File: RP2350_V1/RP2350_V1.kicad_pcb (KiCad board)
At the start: 4 copper layers, 65.3 x 95.8 mm, 107 parts, among them IC1 DMP1045U-7, IC2 DMP1045U-7, IC3 DMP1045U-7, J1 Conn_01x04_Pin, J2 Conn_01x08_Socket, J3 USB_C_Receptacle_USB2.0_16P, J4 Conn_01x08_Socket, J5 Conn_01x08_Socket, J6 Conn_01x02_Pin, J7 Conn_01x04_Pin, SW1 PTS 647 SN50 SMTR2 LFS, SW10 PTS 647 SN50 SMTR2 LFS, SW11 PTS 647 SN50 SMTR2 LFS, SW12 PTS 647 SN50 SMTR2 LFS, SW13 PTS 647 SN50 SMTR2 LFS, SW14 PTS 647 SN50 SMTR2 LFS, SW4 PTS 647 SN50 SMTR2 LFS, SW9 PTS 647 SN50 SMTR2 LFS, U1 RP2350_60QFN, U2 W25Q128JVS, U3 TPS62811QWRWYRQ1, U4 MCP73812T-420I-OT, U5 TLV3012AIDCKR, U6 74HC14, X1 ABM8-272-T3

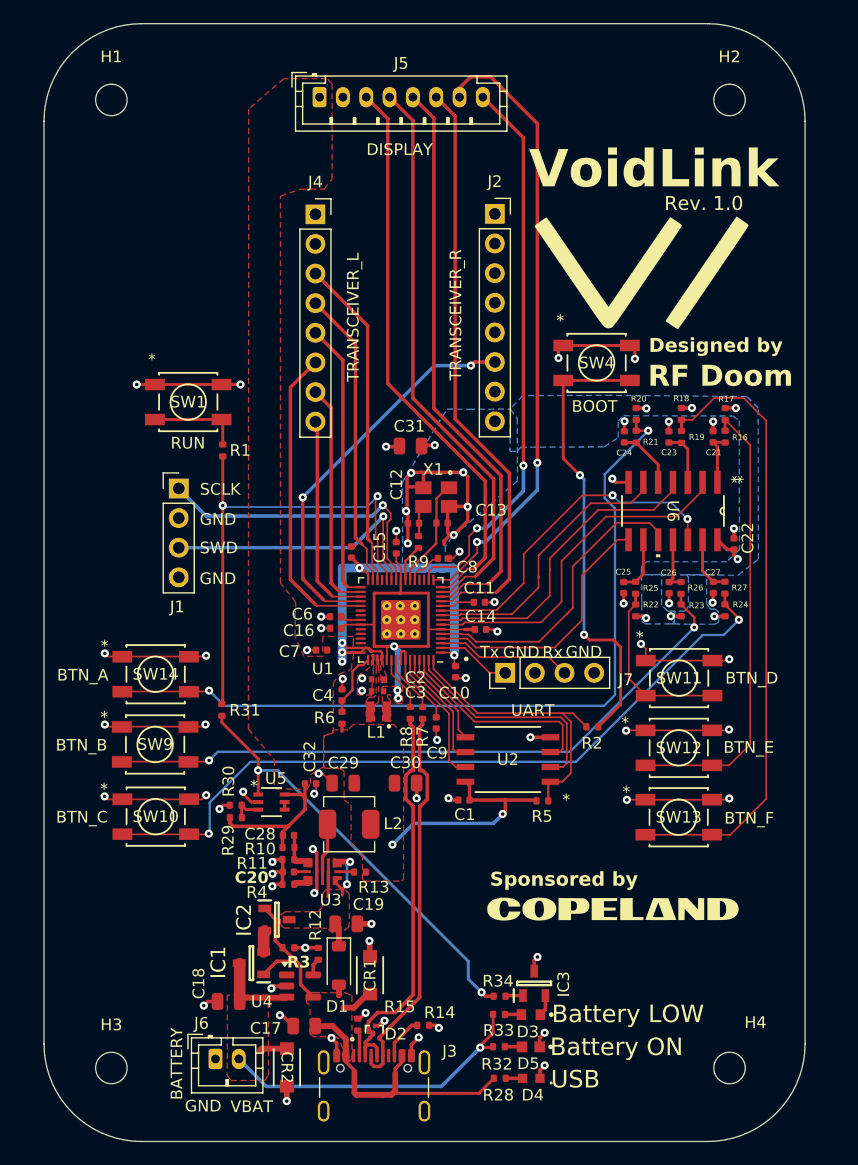
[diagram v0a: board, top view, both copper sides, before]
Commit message: updated manufacturing files, added orientation marker to TPS62811 in lay, no fiducial markers
jlcpcb engineer asked me to confirm the orientation of the tps ic, i guess thats why we use pin 1 markers (flushed.png)
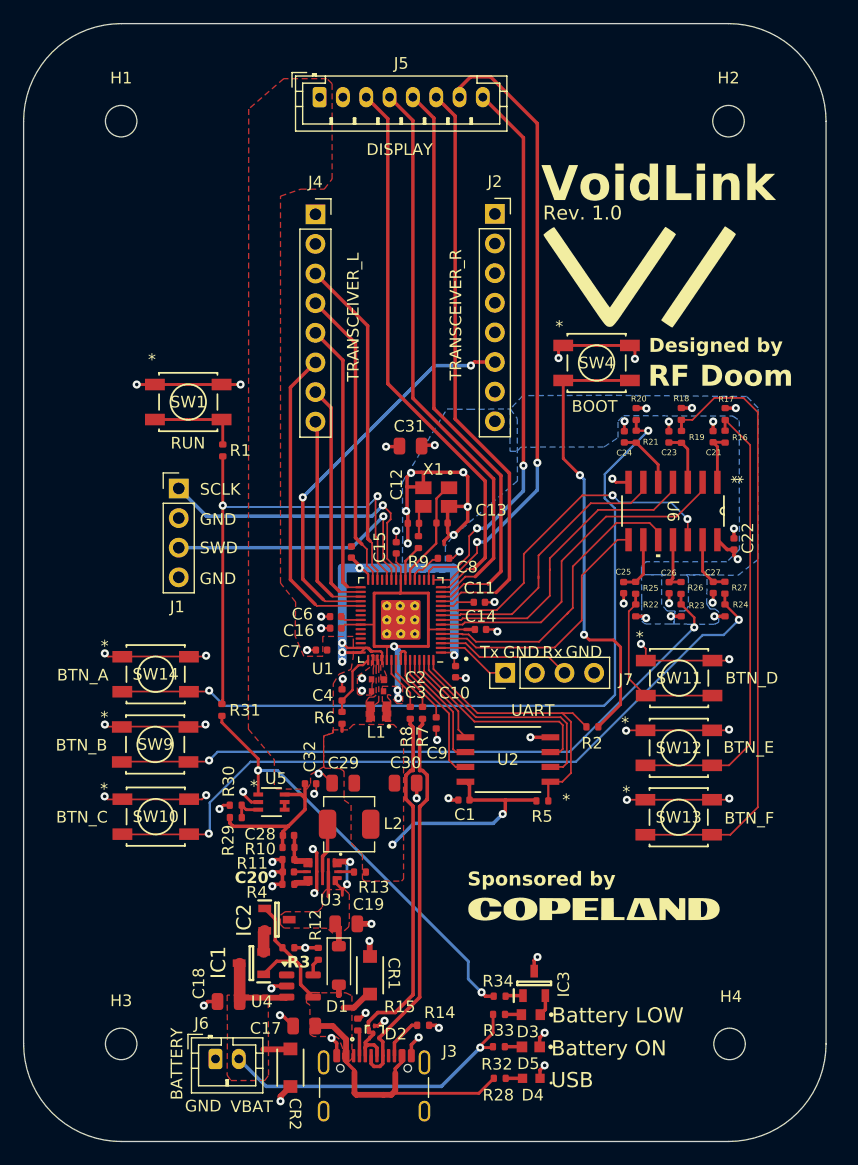
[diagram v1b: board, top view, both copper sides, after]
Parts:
- R28: value 85 -> 86.6
- R32: value 73.3 -> 75
- R33: value 88 -> 88.7
- moved H3 2.23 mm to (120.8, 118.9)
- moved H4 2.06 mm to (173.0, 118.9)
- moved H1 2.00 mm to (120.8, 39.8)
- moved H2 1.82 mm to (172.9, 39.8)
- moved G*** 1.62 mm to (161.4, 107.4)
- moved G*** 0.39 mm to (165.3, 53.2)
- moved CR2 0.30 mm to (135.3, 121.0)
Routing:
- net Net-(R18-Pad2): track 53.9 -> 53.4 mm
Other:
- board size 65.3 x 95.8 mm -> 68.8 x 95.8 mm

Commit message: MAJOR FIX - RP2350 unconnected 3V3, GND  pins - previous versions will NOT work
rip
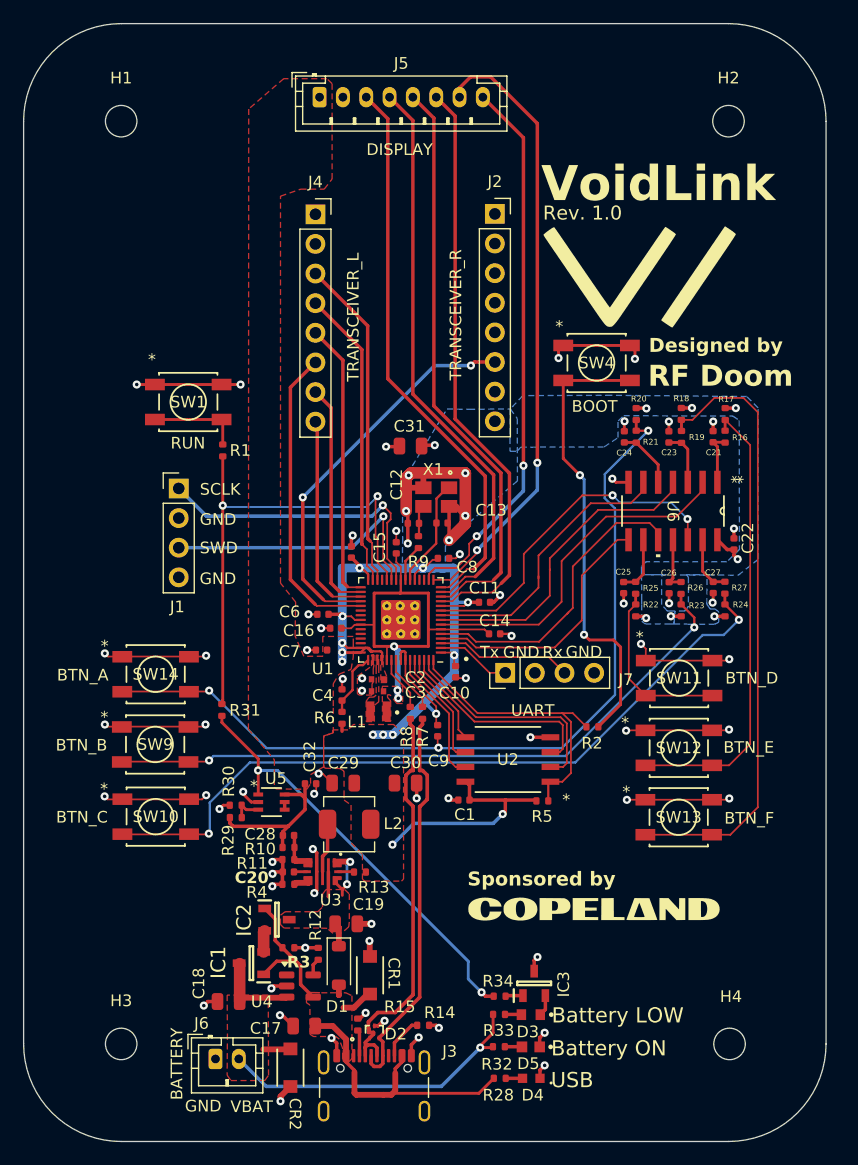
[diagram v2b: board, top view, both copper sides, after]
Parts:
- moved C14 1.27 mm to (152.9, 83.8)
- moved C6 1.11 mm to (138.1, 82.1)
- moved C9 0.68 mm to (148.0, 92.1)
- moved C11 0.44 mm to (152.0, 81.1)
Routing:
- net +3V3: track 95.9 -> 111.6 mm, vias 15 -> 22
- net Net-(R20-Pad2): track 69.9 -> 72.9 mm
- net GND: track 154.0 -> 156.6 mm, vias 70 -> 71
- net +1V1: track 35.0 -> 36.4 mm
- net /DISPLAY_BUSY: track 47.9 -> 47.3 mm

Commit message: now rev1.1; improvements to 1v1 net, cleanup, local drc looks good
lmnop
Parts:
- removed ?: , clipboard:0d6e4b69-4cda-4f93-960e-84a3754837eb
- moved J7 1.02 mm to (154.7, 87.6)
- moved C14 0.57 mm to (153.4, 83.7)
- moved C9 0.35 mm to (148.3, 92.1)
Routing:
- net +1V1: track 36.4 -> 52.9 mm, vias 3 -> 6
- net Net-(R20-Pad2): track 72.9 -> 75.2 mm
- net /BTN_BACK: track 30.0 -> 27.9 mm
- net /BTN_OK: track 27.1 -> 25.2 mm
- net /BTN_NEXT: track 24.3 -> 22.5 mm
- net Net-(U5-IN-): track 0.65 -> 2.39 mm
- net /BTN_MACRO_C: track 29.3 -> 27.9 mm
- net /~{USB_BOOT}: track 39.5 -> 38.2 mm
- net /UART_Rx_DEBUG: track 11.7 -> 12.7 mm
- net /UART_Tx_DEBUG: track 6.41 -> 7.50 mm
- net GND: track 156.6 -> 157.5 mm
- net Net-(R23-Pad2): track 57.2 -> 57.9 mm
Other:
- board text added: "Rev. 1.1"
- board text removed: "Rev. 1.0"
